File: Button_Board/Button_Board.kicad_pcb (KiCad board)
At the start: 2 copper layers, 8 parts, among them J1 Conn_01x10, SW1 SW_Push, SW2 SW_Push, SW3 SW_Push, SW4 SW_Push, SW5 SW_Push, SW6 SW_Push, SW7 SW_Push

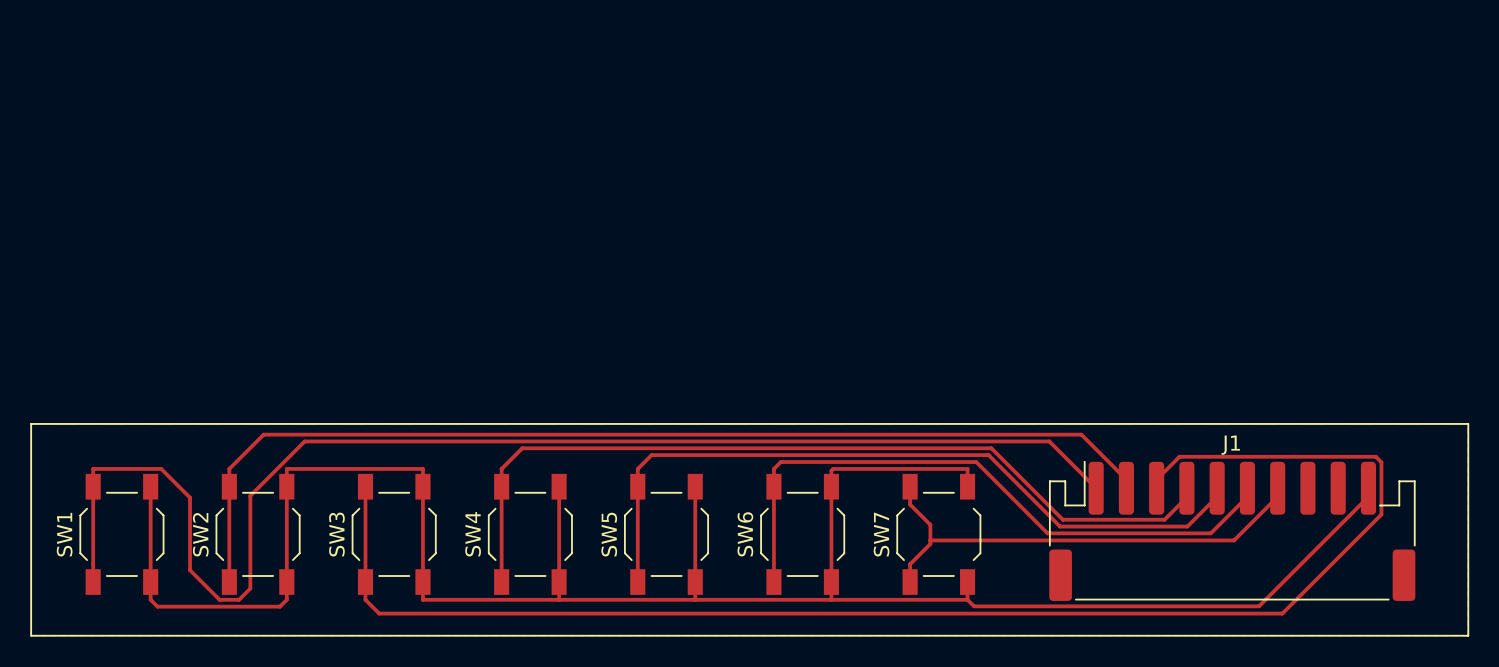
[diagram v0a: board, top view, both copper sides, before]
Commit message: Button board layout with mini joystick
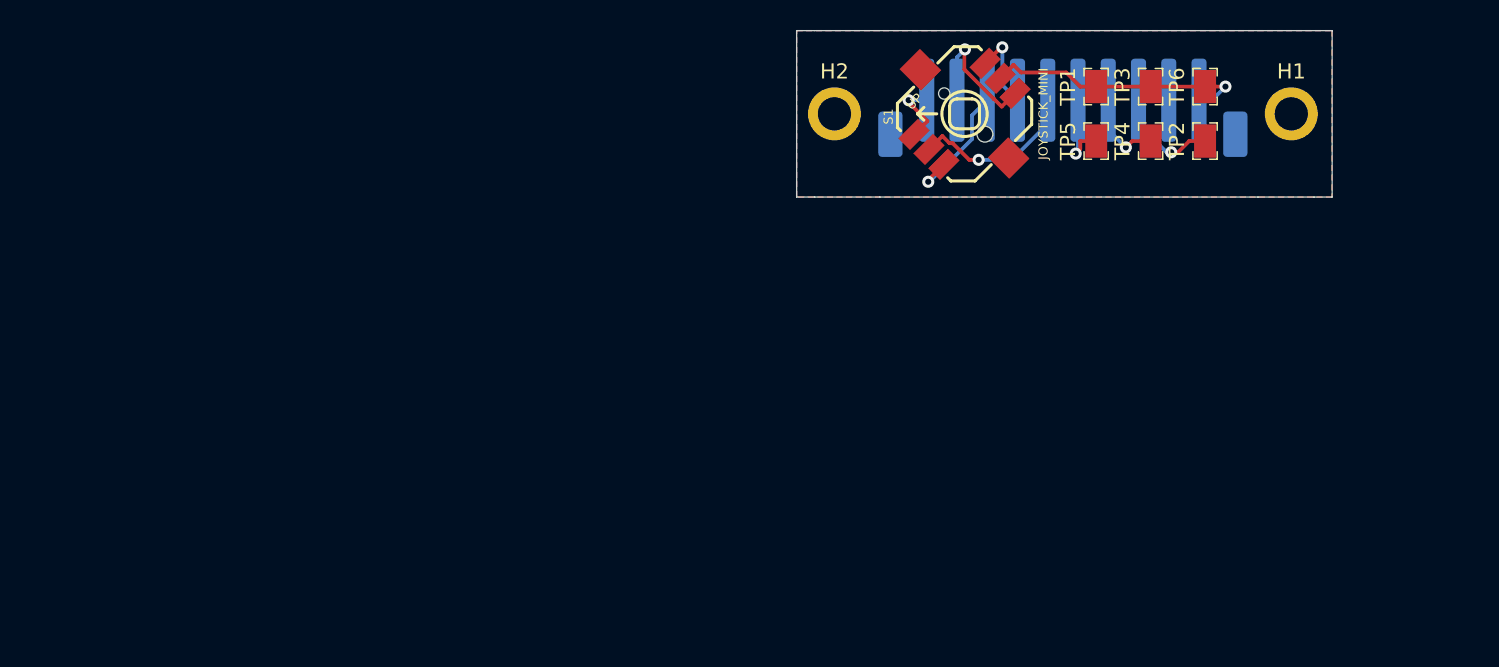
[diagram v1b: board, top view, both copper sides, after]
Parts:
- removed SW1, SW2, SW3, SW4, SW5, SW6, SW7: SW_Push, Button_Switch_SMD:SW_SPST_TL3342
- added H1: MountingHole, MountingHole:MountingHole_2.2mm_M2_ISO7380_Pad, F.Cu at (143.3, 39.5)
- added H2: MountingHole, MountingHole:MountingHole_2.2mm_M2_ISO7380_Pad, F.Cu at (113.1, 39.5)
- added S1: JOYSTICK_MINI, Switches:JOYSTICK_MINI, F.Cu at (121.7, 39.5)
- added TP1: RCT-0C, digikey-footprints:PROBE_PAD_0805, F.Cu at (130.4, 37.7)
- added TP2: RCT-0C, digikey-footprints:PROBE_PAD_0805, F.Cu at (137.6, 41.3)
- added TP3: RCT-0C, digikey-footprints:PROBE_PAD_0805, F.Cu at (134.0, 37.7)
- added TP4: RCT-0C, digikey-footprints:PROBE_PAD_0805, F.Cu at (134.0, 41.3)
- added TP5: RCT-0C, digikey-footprints:PROBE_PAD_0805, F.Cu at (130.4, 41.3)
- added TP6: RCT-0C, digikey-footprints:PROBE_PAD_0805, F.Cu at (137.6, 37.7)
- J1: footprint Connector_JST:JST_PH_S10B-PH-SM4-TB_1x10-1MP_P2.00mm_Horizontal -> Connector_JST:JST_PH_B10B-PH-SM4-TB_1x10-1MP_P2.00mm_Vertical; moved to B.Cu
- moved J1 30.2 mm to (128.2, 39.1)
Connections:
- J1 pad 8: (no net) -> Net-(J1-Pad8)
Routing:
- net GND: track 144.3 -> 18.0 mm, vias 0 -> 1
- net Net-(J1-Pad3): track 97.4 -> 8.63 mm, vias 0 -> 1
- net Net-(J1-Pad1): track 89.4 -> 4.34 mm, vias 0 -> 1
- net Net-(J1-Pad2): track 69.5 -> 9.66 mm, vias 0 -> 1
- net Net-(J1-Pad4): track 56.5 -> 5.48 mm, vias 0 -> 1
- net Net-(J1-Pad5): track 49.5 -> 11.4 mm, vias 0 -> 1
- net Net-(J1-Pad6): track 42.5 -> 5.59 mm, vias 0 -> 1
- net Net-(J1-Pad7): track 32.1 -> 5.41 mm, vias 0 -> 1
- net Net-(J1-Pad8): track 0.00 -> 7.06 mm, vias 0 -> 1
- added copper zone on B.Cu, net GND
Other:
- board outline added: 35.4 x 11 mm
